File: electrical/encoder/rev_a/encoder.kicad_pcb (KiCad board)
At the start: 2 copper layers, 14.8 x 48 mm, 5 parts, among them CN1 ENCODER;2xM1x3RA, Q1 AH1806;SC59, Q2 AH1806;SC59

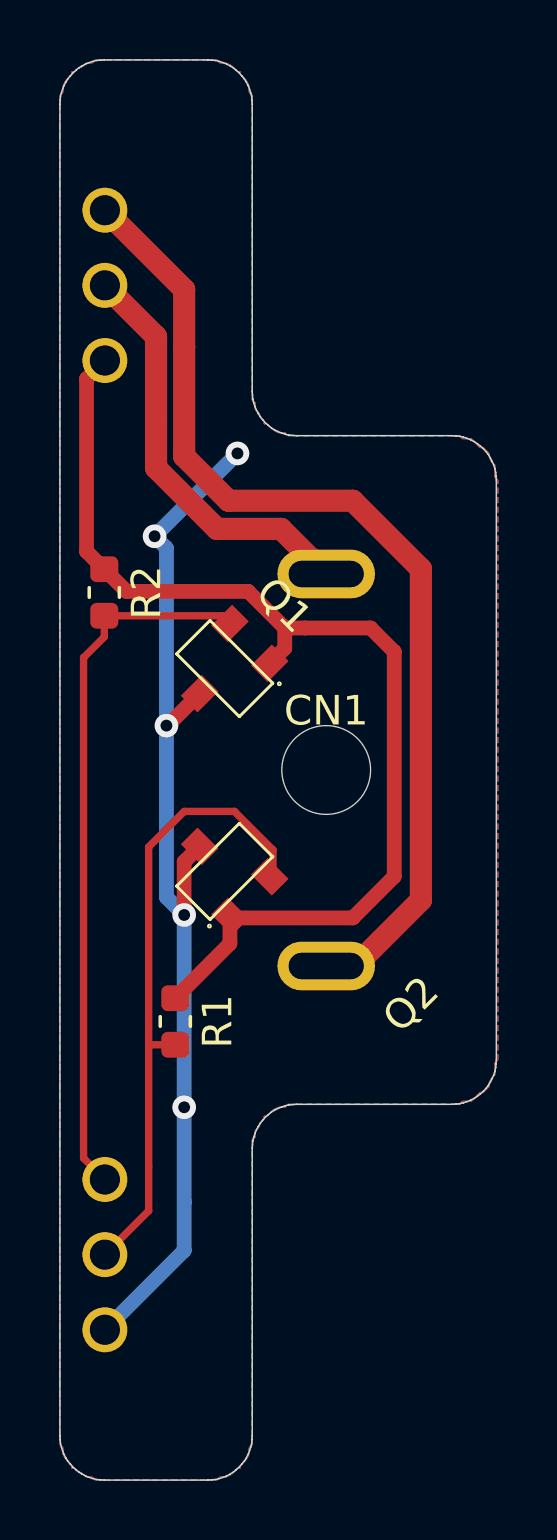
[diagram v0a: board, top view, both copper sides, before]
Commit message: Changes to encoder and st_adapter
Changed AH1806 symbol in encoder.sch
Changed resistor sizes in encoder sch and pcb
Kicad migrated st_adapter sch to new format
Added part designations to st_adapter pcb
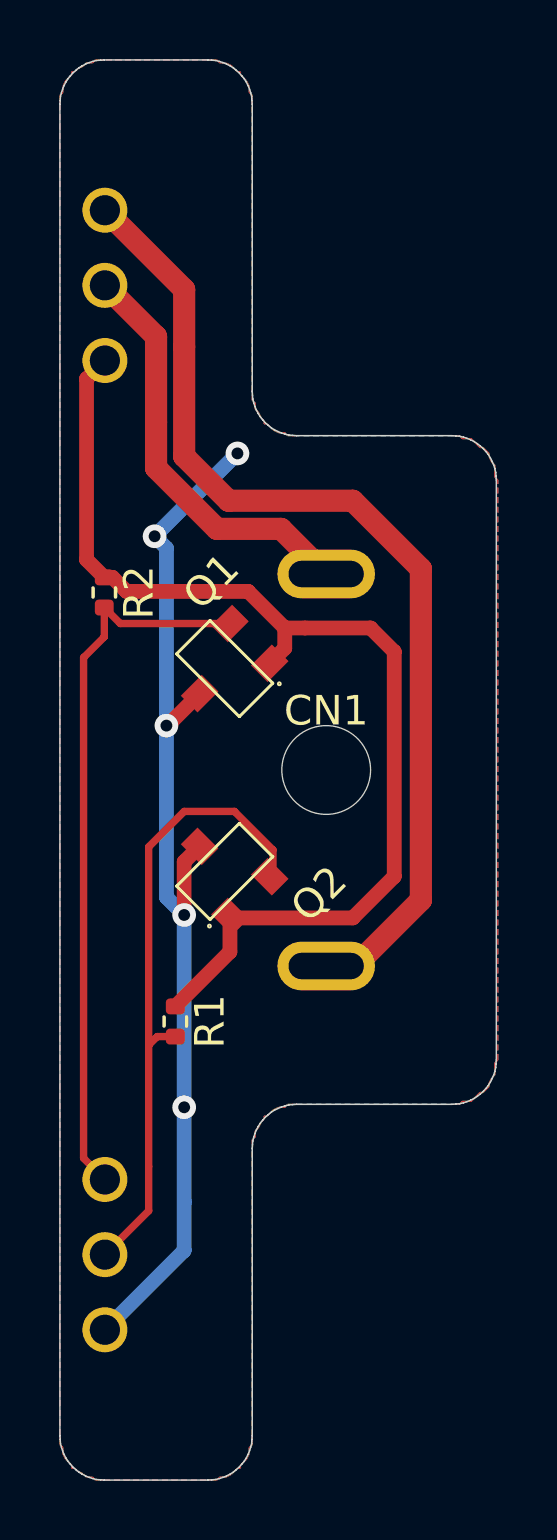
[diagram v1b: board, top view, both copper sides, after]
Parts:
- R1, R2: value 100Ω;1608 -> 100Ω;1005; footprint Resistor_SMD:R_0603_1608Metric -> Resistor_SMD:R_0402_1005Metric

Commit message: Swept through JLCPCB BOM again.
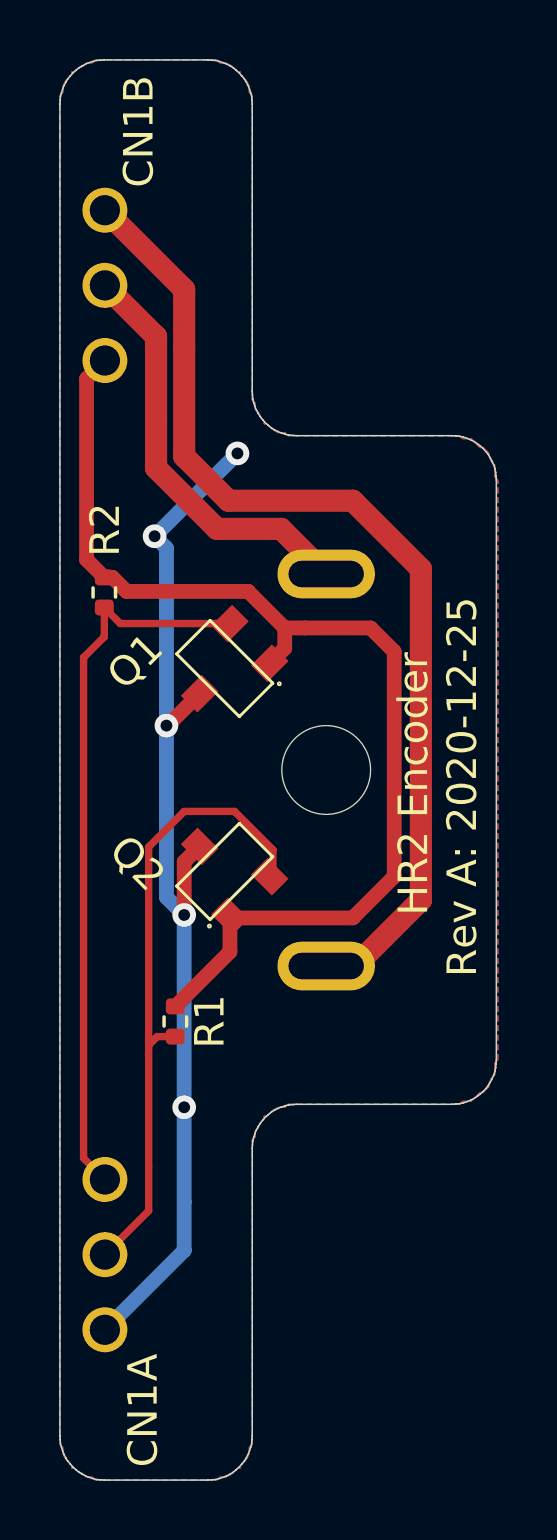
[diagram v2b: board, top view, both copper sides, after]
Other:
- board text added: "A"
- board text added: "CN1B"
- board text added: "HR2 Encoder"
- board text added: "Rev A: 2020-12-25"

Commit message: Genereated gerbers for ST Adapter and Encoder.
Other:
- board text added: "Rev A: 2020DEC26"
- board text removed: "Rev A: 2020-12-25"
